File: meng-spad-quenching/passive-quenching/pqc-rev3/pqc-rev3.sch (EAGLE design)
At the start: 62 parts, among them IC1 TPS7A4901, IC2 OPA858, IC3 OPA858, IC4 LM8261, Q1 NTR5105P, Q2 BSS123LT1G, Q3 NUD3160LT1G, X1 VIN_BIAS, X2 SPAD, X3 SIGNAL_OUT, X4 VIN_PWR

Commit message: Fixed filenames
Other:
- moved on the sheet: C1, C10, C11, C12, C13, C14, C15, C16, C17, C18, C19, C2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

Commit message: work on BOMs
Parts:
- C12: value C_TUNE1 -> DNP
- C14: value C_TUNE2 -> DNP
- C17: value C_SNS -> CAP CER 10PF 250V C0G/NP0 0603
- C19: value C_FB2 -> DNP
- C20: value C_FB1 -> CAP CER 0.1PF 50V C0G/NP0 0402
- C3: value CAP CER 10000PF 25V X7R 0603 10% -> DNP
- D1: value DF2B36FU,H3F -> D55V0M1B2WS-7
- D3: value DF2B36FU,H3F -> DNP
- IC1: value TPS7A4901 -> TPS79850
- IC2: value OPA858 -> DNP
- R1: value RES SMD 76.8K OHM 1% 1/10W 0603 -> 0R JUMPER 0603
- R10: value R_FB2 -> RES SMD 100 OHM 1% 0402
- R11: value R_FB1 -> RES SMD 1K OHM 1% 0402
- R3: value RES SMD 24K OHM 1% 1/10W 0603 -> DNP
- R4: value R_TIA -> DNP
- R5: value R_Q -> RES SMD 100K OHM 1% 0805
- R6: value R_SNS1 -> DNP
- R7: value RES SMD 50 OHM 1% 0603 -> DNP
- R8: value R_SNS -> RES SMD 50 OHM 1% 0402
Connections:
- net LDO_P5V0_NR_SS_CH1 renamed LDO_P5V0_NR_SS
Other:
- note added: "Compensation Cap (RF/Hi-Q)"
- note added: "ESD 55V standoff, 57V breakdown (min), 100V clamping (max)"
- note added: "Midrail reference buffer Stable under any cap load"
- note added: "Quench Resistor"
- note added: "Sense Resistor"
- note added: "Signal Coupling Cap (RF/Hi-Q)"
- note added: "TPS7A4901: R1 = 76.8K C3 = 10nF C3 = 24K Vout = 5V"
- note added: "This package pinout works for various MSOP8 Power Pad high-voltage LDOs. Checked: LT3010-5 (10k-100k = 100uVrms noise) TPS79850 (10k-100k = 100uVrms noise) TPS7A4901 (35V MAX INPUT!)"
- note removed: "ESD Update MPN for 50V"
- note removed: "Midrail reference buffer"
- note removed: "This package pinout works for various MSOP8 Power Pad high-voltage LDOs. Checked: LT3010-5 (10k-100k = 100uVrms noise) TPS79850 (10k-100k = 100uVrms noise)"
- moved on the sheet: C10, C11, C13, C18, C21, C22, C8, D2, D4, D5, IC2, IC3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

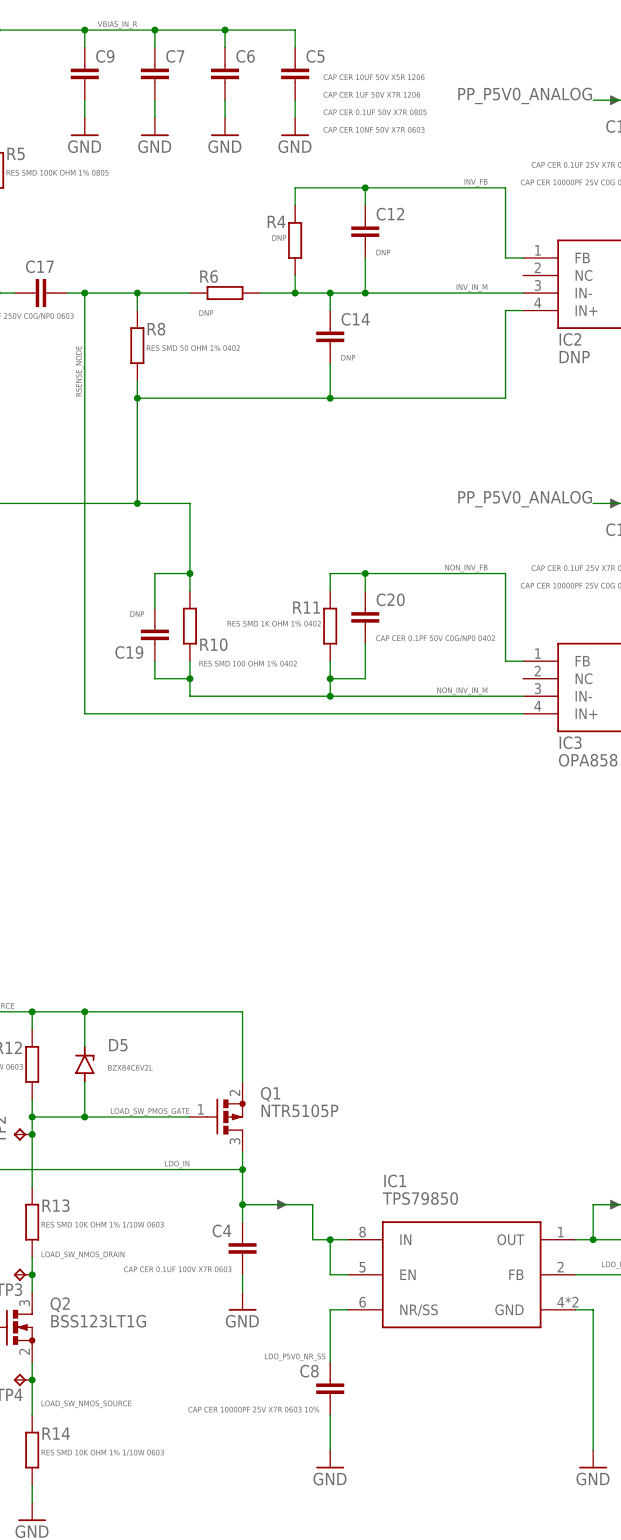
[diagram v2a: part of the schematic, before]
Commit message: Started aqc-rev4 design files by copying over aqc-rev3
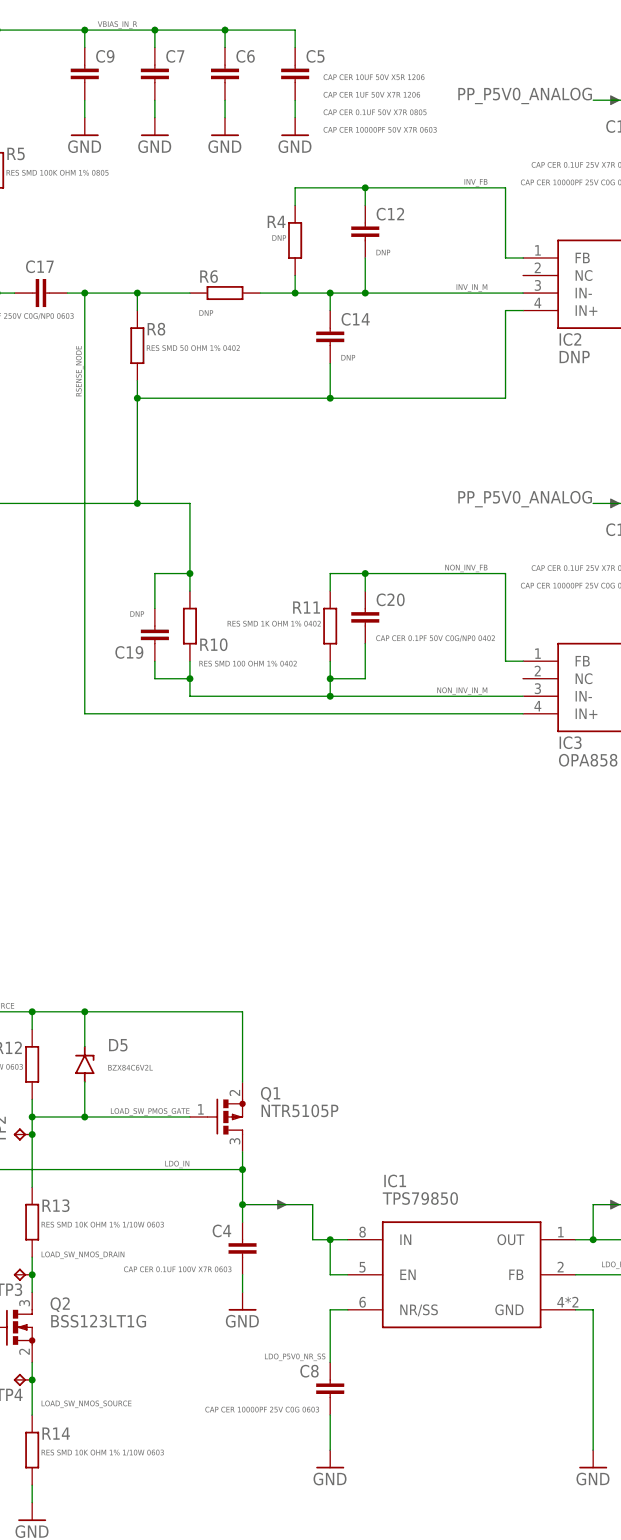
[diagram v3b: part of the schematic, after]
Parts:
- C8: value CAP CER 10000PF 25V X7R 0603 10% -> CAP CER 10000PF 25V C0G 0603
- C9: value CAP CER 10NF 50V X7R 0603 -> CAP CER 10000PF 50V X7R 0603
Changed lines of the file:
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@@
 <part name="U$58" library="Kramnik's Library" deviceset="LEFT_ARROW" device=""/>
 <part name="U$286" library="Kramnik's Library" deviceset="LEFT_ARROW" device=""/>
-<part name="C8" library="rcl-modified-footprints" deviceset="C-EU" device="C0603" package3d_urn="urn:adsk.eagle:package:23616/2" value="CAP CER 10000PF 25V X7R 0603 10%"/>
+<part name="C8" library="rcl-modified-footprints" deviceset="C-EU" device="C0603" package3d_urn="urn:adsk.eagle:package:23616/2" value="CAP CER 10000PF 25V C0G 0603"/>
 <part name="GND144" library="supply1" deviceset="GND" device=""/>
 <part name="GND145" library="supply1" deviceset="GND" device=""/>
@@
 <part name="TP3" library="testpad" library_urn="urn:adsk.eagle:library:385" deviceset="TP" device="TP10R" package3d_urn="urn:adsk.eagle:package:27959/1" value="TPTP10R"/>
 <part name="GND11" library="supply1" deviceset="GND" device=""/>
-<part name="C9" library="rcl-modified-footprints" deviceset="C-EU" device="C0603" package3d_urn="urn:adsk.eagle:package:23616/2" value="CAP CER 10NF 50V X7R 0603"/>
+<part name="C9" library="rcl-modified-footprints" deviceset="C-EU" device="C0603" package3d_urn="urn:adsk.eagle:package:23616/2" value="CAP CER 10000PF 50V X7R 0603"/>
 <part name="FRAME1" library="frames" library_urn="urn:adsk.eagle:library:229" deviceset="FRAME_B_L" device=""/>
 <part name="DNP9" library="meng" deviceset="ARROW_1DIR" device=""/>

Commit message: misc sync
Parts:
- IC2: value DNP -> OPA858
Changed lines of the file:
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@@
 <grid distance="0.1" unitdist="inch" unit="inch" style="lines" multiple="1" display="no" altdistance="0.01" altunitdist="inch" altunit="inch"/>
 <layers>
-<layer number="1" name="Top" color="4" fill="1" visible="yes" active="no"/>
-<layer number="2" name="Route2" color="3" fill="1" visible="yes" active="no"/>
-<layer number="3" name="Route3" color="4" fill="3" visible="yes" active="no"/>
-<layer number="4" name="Route4" color="1" fill="4" visible="yes" active="no"/>
-<layer number="5" name="Route5" color="4" fill="4" visible="yes" active="no"/>
-<layer number="6" name="Route6" color="1" fill="8" visible="yes" active="no"/>
-<layer number="7" name="Route7" color="4" fill="8" visible="yes" active="no"/>
-<layer number="8" name="Route8" color="1" fill="2" visible="yes" active="no"/>
-<layer number="9" name="Route9" color="4" fill="2" visible="yes" active="no"/>
-<layer number="10" name="Route10" color="1" fill="7" visible="yes" active="no"/>
-<layer number="11" name="Route11" color="4" fill="7" visible="yes" active="no"/>
-<layer number="12" name="Route12" color="1" fill="5" visible="yes" active="no"/>
-<layer number="13" name="Route13" color="4" fill="5" visible="yes" active="no"/>
-<layer number="14" name="Route14" color="1" fill="6" visible="yes" active="no"/>
-<layer number="15" name="Route15" color="6" fill="1" visible="yes" active="no"/>
-<layer number="16" name="Bottom" color="1" fill="1" visible="yes" active="no"/>
-<layer number="17" name="Pads" color="2" fill="1" visible="yes" active="no"/>
-<layer number="18" name="Vias" color="2" fill="1" visible="yes" active="no"/>
-<layer number="19" name="Unrouted" color="6" fill="1" visible="yes" active="no"/>
-<layer number="20" name="Dimension" color="24" fill="1" visible="yes" active="no"/>
-<layer number="21" name="tPlace" color="7" fill="1" visible="yes" active="no"/>
-<layer number="22" name="bPlace" color="7" fill="1" visible="yes" active="no"/>
-<layer number="23" name="tOrigins" color="15" fill="1" visible="yes" active="no"/>
-<layer number="24" name="bOrigins" color="15" fill="1" visible="yes" active="no"/>
-<layer number="25" name="tNames" color="7" fill="1" visible="yes" active="no"/>
-<layer number="26" name="bNames" color="7" fill="1" visible="yes" active="no"/>
-<layer number="27" name="tValues" color="7" fill="1" visible="yes" active="no"/>
-<layer number="28" name="bValues" color="7" fill="1" visible="yes" active="no"/>
+<layer number="1" name="Top" color="4" fill="1" visible="no" active="no"/>
+<layer number="2" name="Route2" color="3" fill="1" visible="no" active="no"/>
+<layer number="3" name="Route3" color="4" fill="3" visible="no" active="no"/>
+<layer number="4" name="Route4" color="1" fill="4" visible="no" active="no"/>
+<layer number="5" name="Route5" color="4" fill="4" visible="no" active="no"/>
+<layer number="6" name="Route6" color="1" fill="8" visible="no" active="no"/>
+<layer number="7" name="Route7" color="4" fill="8" visible="no" active="no"/>
+<layer number="8" name="Route8" color="1" fill="2" visible="no" active="no"/>
+<layer number="9" name="Route9" color="4" fill="2" visible="no" active="no"/>
+<layer number="10" name="Route10" color="1" fill="7" visible="no" active="no"/>
+<layer number="11" name="Route11" color="4" fill="7" visible="no" active="no"/>
+<layer number="12" name="Route12" color="1" fill="5" visible="no" active="no"/>
+<layer number="13" name="Route13" color="4" fill="5" visible="no" active="no"/>
+<layer number="14" name="Route14" color="1" fill="6" visible="no" active="no"/>
+<layer number="15" name="Route15" color="6" fill="1" visible="no" active="no"/>
+<layer number="16" name="Bottom" color="1" fill="1" visible="no" active="no"/>
+<layer number="17" name="Pads" color="2" fill="1" visible="no" active="no"/>
+<layer number="18" name="Vias" color="2" fill="1" visible="no" active="no"/>
+<layer number="19" name="Unrouted" color="6" fill="1" visible="no" active="no"/>
+<layer number="20" name="Dimension" color="24" fill="1" visible="no" active="no"/>
+<layer number="21" name="tPlace" color="7" fill="1" visible="no" active="no"/>
+<layer number="22" name="bPlace" color="7" fill="1" visible="no" active="no"/>
+<layer number="23" name="tOrigins" color="15" fill="1" visible="no" active="no"/>
+<layer number="24" name="bOrigins" color="15" fill="1" visible="no" active="no"/>
+<layer number="25" name="tNames" color="7" fill="1" visible="no" active="no"/>
+<layer number="26" name="bNames" color="7" fill="1" visible="no" active="no"/>
+<layer number="27" name="tValues" color="7" fill="1" visible="no" active="no"/>
+<layer number="28" name="bValues" color="7" fill="1" visible="no" active="no"/>
 <layer number="29" name="tStop" color="7" fill="3" visible="no" active="no"/>
 <layer number="30" name="bStop" color="7" fill="6" visible="no" active="no"/>
@@
 <layer number="35" name="tGlue" color="7" fill="4" visible="no" active="no"/>
 <layer number="36" name="bGlue" color="7" fill="5" visible="no" active="no"/>
-<layer number="37" name="tTest" color="7" fill="1" visible="yes" active="no"/>
-<layer number="38" name="bTest" color="7" fill="1" visible="yes" active="no"/>
+<layer number="37" name="tTest" color="7" fill="1" visible="no" active="no"/>
+<layer number="38" name="bTest" color="7" fill="1" visible="no" active="no"/>
 <layer number="39" name="tKeepout" color="4" fill="11" visible="no" active="no"/>
 <layer number="40" name="bKeepout" color="1" fill="11" visible="no" active="no"/>
@@
 <layer number="44" name="Drills" color="7" fill="1" visible="no" active="no"/>
 <layer number="45" name="Holes" color="7" fill="1" visible="no" active="no"/>
-<layer number="46" name="Milling" color="3" fill="1" visible="yes" active="no"/>
-<layer number="47" name="Measures" color="7" fill="1" visible="yes" active="no"/>
-<layer number="48" name="Document" color="7" fill="1" visible="yes" active="no"/>
-<layer number="49" name="Reference" color="7" fill="1" visible="yes" active="no"/>
-<layer number="50" name="dxf" color="7" fill="1" visible="yes" active="no"/>
-<layer number="51" name="tDocu" color="7" fill="1" visible="yes" active="no"/>
-<layer number="52" name="bDocu" color="7" fill="1" visible="yes" active="no"/>
-<layer number="53" name="tPadExt" color="7" fill="1" visible="yes" active="no"/>
-<layer number="54" name="bPadExt" color="1" fill="1" visible="yes" active="no"/>
-<layer number="56" name="wert" color="7" fill="1" visible="yes" active="no"/>
-<layer number="57" name="tCAD" color="7" fill="1" visible="yes" active="no"/>
-<layer number="59" name="tCarbon" color="7" fill="1" visible="yes" active="no"/>
-<layer number="60" name="bCarbon" color="7" fill="1" visible="yes" active="no"/>
+<layer number="46" name="Milling" color="3" fill="1" visible="no" active="no"/>
+<layer number="47" name="Measures" color="7" fill="1" visible="no" active="no"/>
+<layer number="48" name="Document" color="7" fill="1" visible="no" active="no"/>
+<layer number="49" name="Reference" color="7" fill="1" visible="no" active="no"/>
+<layer number="50" name="dxf" color="7" fill="1" visible="no" active="no"/>
+<layer number="51" name="tDocu" color="7" fill="1" visible="no" active="no"/>
+<layer number="52" name="bDocu" color="7" fill="1" visible="no" active="no"/>
+<layer number="53" name="tPadExt" color="7" fill="1" visible="no" active="no"/>
+<layer number="54" name="bPadExt" color="1" fill="1" visible="no" active="no"/>
+<layer number="56" name="wert" color="7" fill="1" visible="no" active="no"/>
+<layer number="57" name="tCAD" color="7" fill="1" visible="no" active="no"/>
+<layer number="59" name="tCarbon" color="7" fill="1" visible="no" active="no"/>
+<layer number="60" name="bCarbon" color="7" fill="1" visible="no" active="no"/>
 <layer number="88" name="SimResults" color="9" fill="1" visible="yes" active="yes"/>
 <layer number="89" name="SimProbes" color="9" fill="1" visible="yes" active="yes"/>
@@
 <part name="C12" library="rcl-modified-footprints" deviceset="C-EU" device="C0402" package3d_urn="urn:adsk.eagle:package:23626/1" value="DNP"/>
 <part name="R4" library="rcl-modified-footprints" deviceset="R-EU_" device="R0402" package3d_urn="urn:adsk.eagle:package:23547/1" value="DNP"/>
-<part name="IC2" library="meng" deviceset="OPA858" device="" value="DNP"/>
+<part name="IC2" library="meng" deviceset="OPA858" device="" value="OPA858"/>
 <part name="R7" library="rcl-modified-footprints" deviceset="R-EU_" device="R0603" package3d_urn="urn:adsk.eagle:package:23555/2" value="DNP"/>
 <part name="C14" library="rcl-modified-footprints" deviceset="C-EU" device="C0402" package3d_urn="urn:adsk.eagle:package:23626/1" value="DNP"/>
